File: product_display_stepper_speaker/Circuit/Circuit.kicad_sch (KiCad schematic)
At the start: 1 part, among them U1 Pico

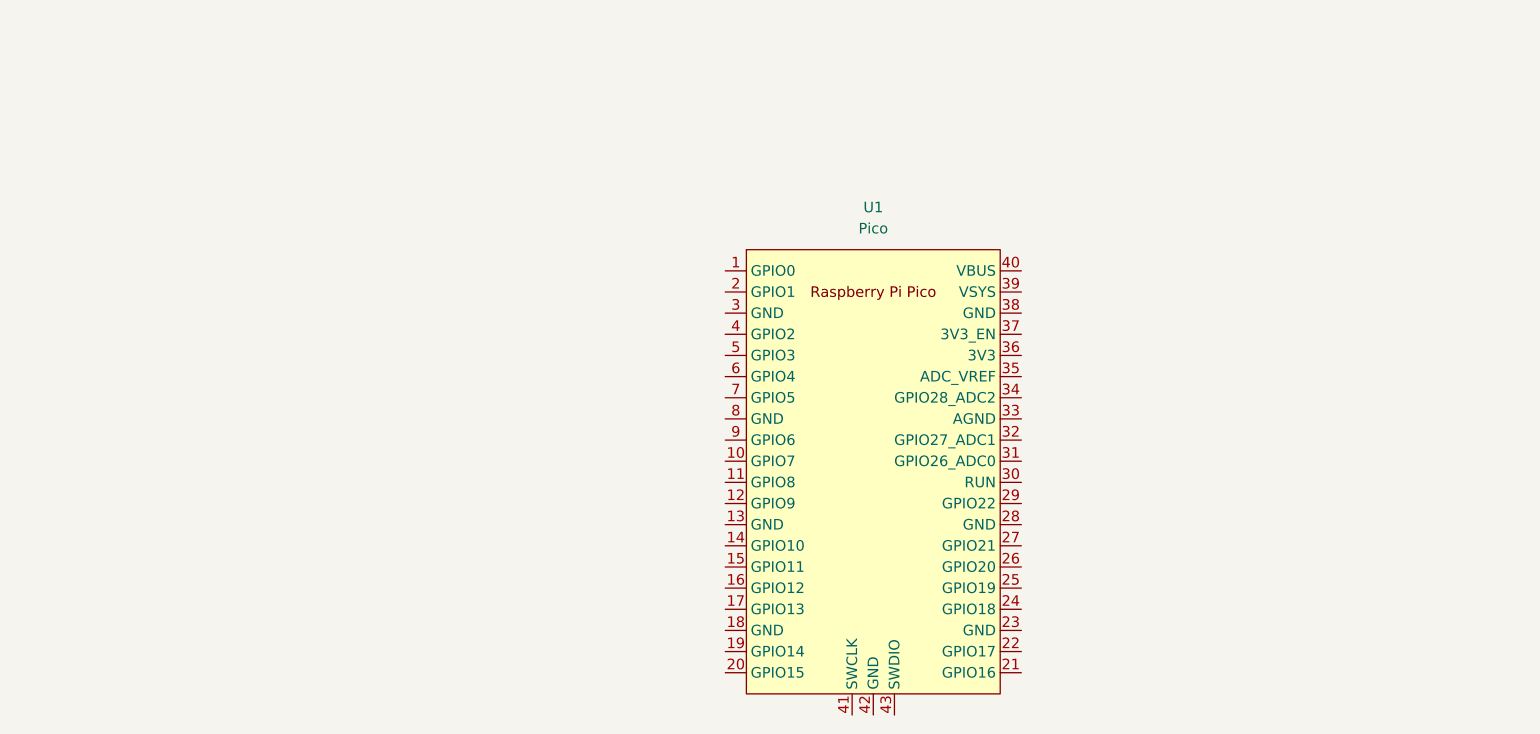
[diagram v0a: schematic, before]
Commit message: finished circuit schematic and started pcb layout of product speaker stepper project
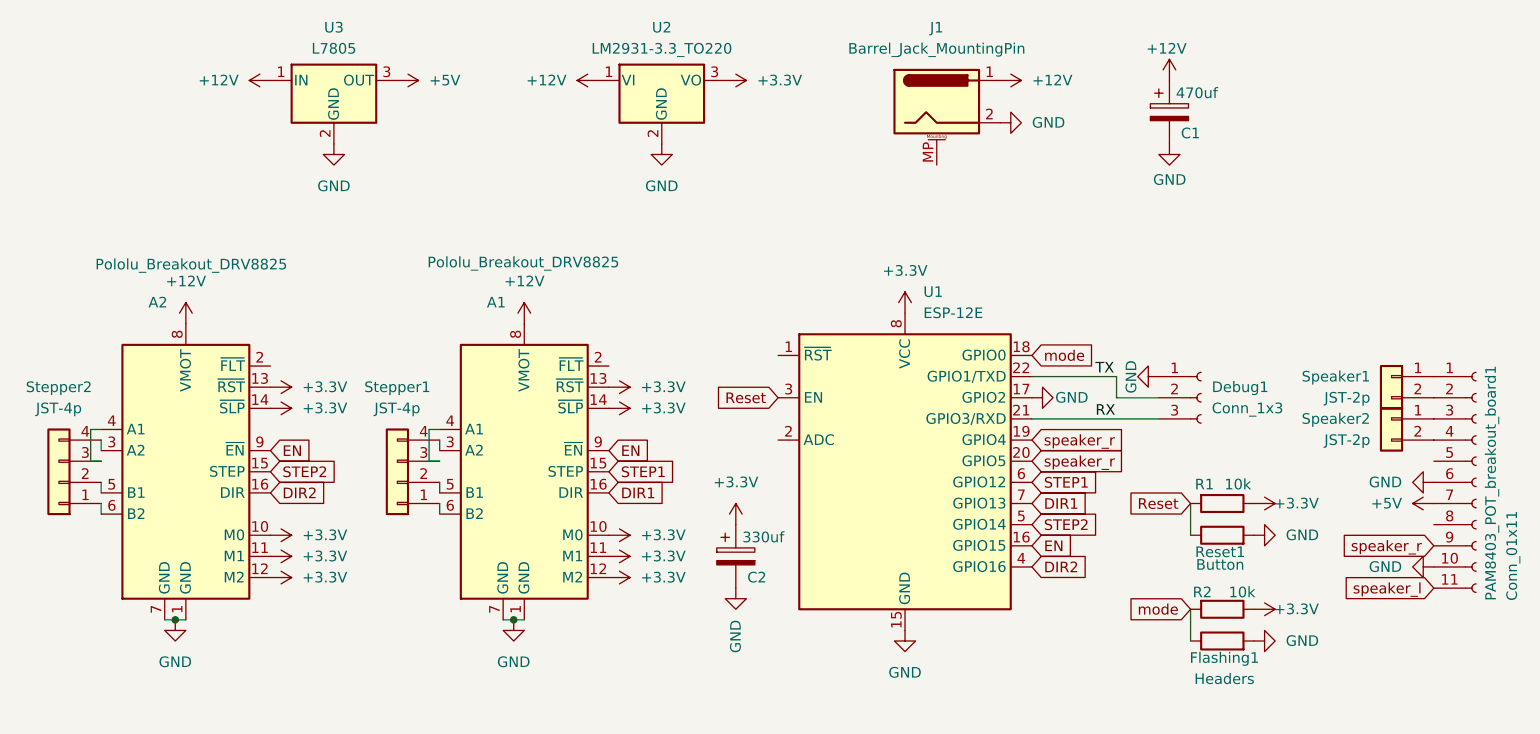
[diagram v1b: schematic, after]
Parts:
- removed U1: Pico, MCU_RaspberryPi_and_Boards:RPi_Pico_SMD_TH, symbol MCU_RaspberryPi_and_Boards:Pico
- added A1, A2: Pololu_Breakout_DRV8825, Module:Pololu_Breakout-16_15.2x20.3mm, symbol Driver_Motor:Pololu_Breakout_DRV8825
- added C1: 470uf, Capacitor_THT:C_Radial_D8.0mm_H11.5mm_P3.50mm, symbol Device:C_Polarized
- added C2: 330uf, Capacitor_THT:C_Radial_D8.0mm_H11.5mm_P3.50mm, symbol Device:C_Polarized
- added Debug1: Conn_1x3, Connector_PinHeader_2.54mm:PinHeader_1x03_P2.54mm_Vertical, symbol Connector:Conn_01x03_Socket
- added Flashing1: Headers, Resistor_THT:R_Axial_DIN0207_L6.3mm_D2.5mm_P2.54mm_Vertical, symbol Device:R
- added J1: Barrel_Jack_MountingPin, Connector_BarrelJack:BarrelJack_GCT_DCJ200-10-A_Horizontal, symbol Connector:Barrel_Jack_MountingPin
- added PAM8403_POT_breakout_board1: Conn_01x11, Connector_PinHeader_2.54mm:PinHeader_1x11_P2.54mm_Vertical, symbol Connector:Conn_01x11_Socket
- added R1, R2: 10k, Resistor_THT:R_Axial_DIN0207_L6.3mm_D2.5mm_P7.62mm_Horizontal, symbol Device:R
- added Reset1: Button, Resistor_THT:R_Axial_DIN0207_L6.3mm_D2.5mm_P5.08mm_Vertical, symbol Device:R
- added Speaker1, Speaker2: JST-2p, Connector_JST:JST_EH_B2B-EH-A_1x02_P2.50mm_Vertical, symbol Connector_Generic:Conn_01x02
- added Stepper1, Stepper2: JST-4p, Connector_JST:JST_EH_B4B-EH-A_1x04_P2.50mm_Vertical, symbol Connector_Generic:Conn_01x04
- added U1: ESP-12E, ESP:ESP-12E-DIP, symbol RF_Module:ESP-12E
- added U2: LM2931-3.3_TO220, Package_TO_SOT_THT:TO-220-3_Vertical, symbol Regulator_Linear:LM2931-3.3_TO220
- added U3: L7805, Package_TO_SOT_THT:TO-220-3_Vertical, symbol Regulator_Linear:L7805
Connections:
- new net: PAM8403_POT_breakout_board1.1 (Pin_1), Speaker1.1 (Pin_1)
- new net: PAM8403_POT_breakout_board1.2 (Pin_2), Speaker1.2 (Pin_2)
- new net: PAM8403_POT_breakout_board1.3 (Pin_3), Speaker2.1 (Pin_1)
- new net: PAM8403_POT_breakout_board1.4 (Pin_4), Speaker2.2 (Pin_2)
- new net: A2.3 (A2), Stepper2.4 (Pin_4)
- new net: A2.4 (A1), Stepper2.3 (Pin_3)
- new net: A2.5 (B1), Stepper2.2 (Pin_2)
- new net: A2.6 (B2), Stepper2.1 (Pin_1)
- new net: A1.6 (B2), Stepper1.1 (Pin_1)
- new net: A1.5 (B1), Stepper1.2 (Pin_2)
- new net: A1.4 (A1), Stepper1.3 (Pin_3)
- new net: A1.3 (A2), Stepper1.4 (Pin_4)
- new net +12V: A1.8 (VMOT), A2.8 (VMOT), C1.1, J1.1, U2.1 (VI), U3.1 (IN)
- new net +3.3V: A1.10 (M0), A1.11 (M1), A1.12 (M2), A1.13 (~{RST}), A1.14 (~{SLP}), A2.10 (M0), A2.11 (M1), A2.12 (M2), A2.13 (~{RST}), A2.14 (~{SLP}), C2.1, R1.1, R2.1, U1.8 (VCC), U2.3 (VO)
- new net +5V: PAM8403_POT_breakout_board1.7 (Pin_7), U3.3 (OUT)
- new net DIR1: A1.16 (DIR), U1.7 (GPIO13)
- new net DIR2: A2.16 (DIR), U1.4 (GPIO16)
- new net EN: A1.9 (~{EN}), A2.9 (~{EN}), U1.16 (GPIO15)
- new net GND: A1.1 (GND), A1.7 (GND), A2.1 (GND), A2.7 (GND), C1.2, C2.2, Debug1.1 (Pin_1), Flashing1.2, J1.2, PAM8403_POT_breakout_board1.10 (Pin_10), PAM8403_POT_breakout_board1.6 (Pin_6), Reset1.2, U1.15 (GND), U1.17 (GPIO2), U2.2 (GND), U3.2 (GND)
- new net RX: Debug1.3 (Pin_3), U1.21 (GPIO3/RXD)
- new net Reset: R1.2, Reset1.1, U1.3 (EN)
- new net STEP1: A1.15 (STEP), U1.6 (GPIO12)
- new net STEP2: A2.15 (STEP), U1.5 (GPIO14)
- new net TX: Debug1.2 (Pin_2), U1.22 (GPIO1/TXD)
- new net mode: Flashing1.1, R2.2, U1.18 (GPIO0)
- new net speaker_l: PAM8403_POT_breakout_board1.11 (Pin_11)
- new net speaker_r: PAM8403_POT_breakout_board1.9 (Pin_9), U1.19 (GPIO4), U1.20 (GPIO5)

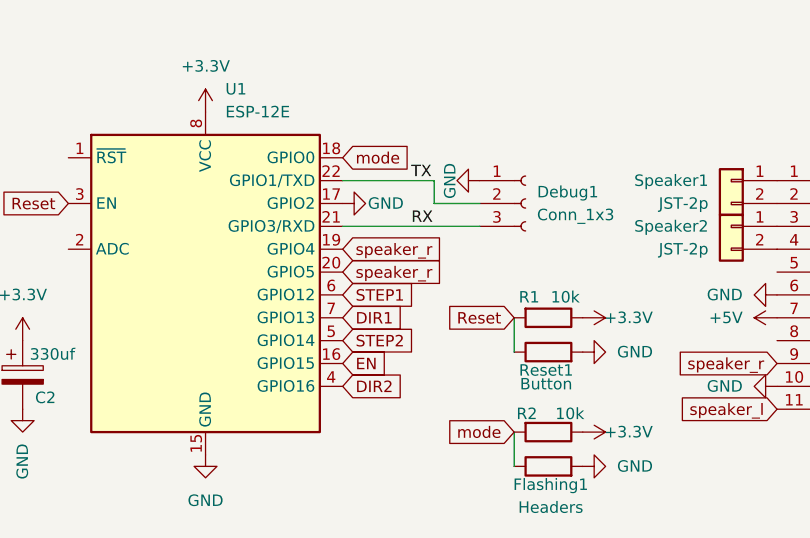
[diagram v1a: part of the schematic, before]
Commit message: almost finished pcb layout solution
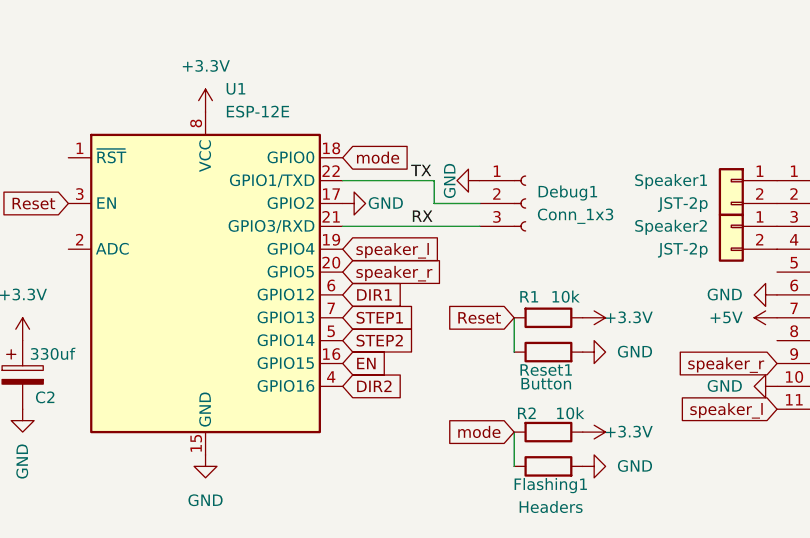
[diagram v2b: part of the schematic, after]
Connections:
- net DIR1: now also U1.6 (GPIO12); no longer U1.7 (GPIO13)
- net STEP1: now also U1.7 (GPIO13); no longer U1.6 (GPIO12)
- net speaker_l: now also U1.19 (GPIO4)
- net speaker_r: no longer U1.19 (GPIO4)
